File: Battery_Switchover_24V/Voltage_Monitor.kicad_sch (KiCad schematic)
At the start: 15 parts, among them Q2 NMOS, Q3 NMOS, Q4 NMOS, Q5 NMOS, Q6 NMOS, Q7 NMOS, U1 LM74610QDGKRQ1, U2 LM74610QDGKRQ1

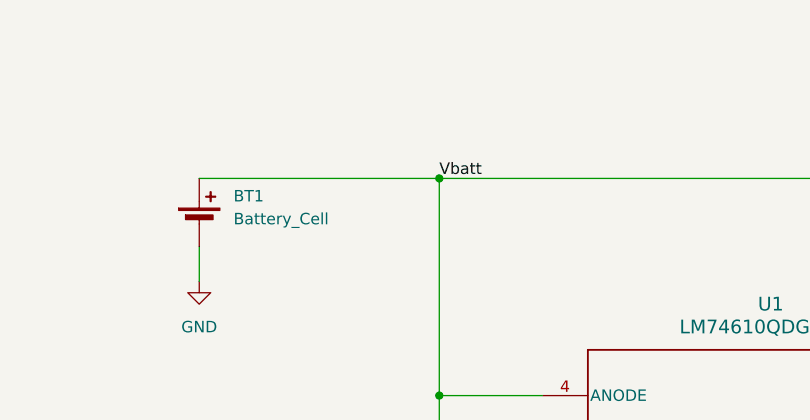
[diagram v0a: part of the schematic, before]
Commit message: Voltaj denetim çipi eklendi
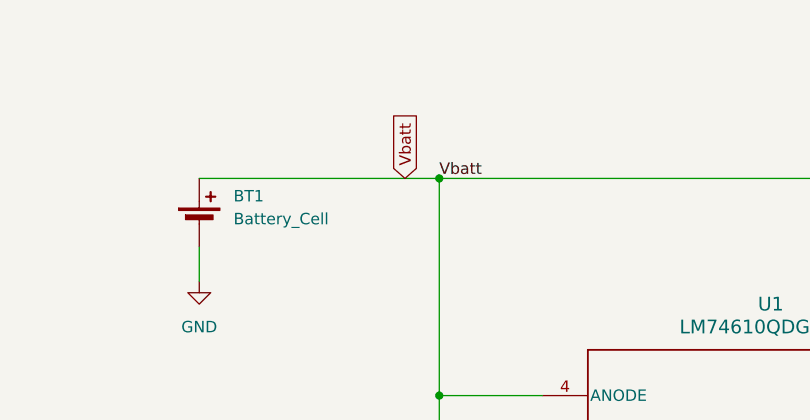
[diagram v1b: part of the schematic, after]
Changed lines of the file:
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@@
+		)
+	)
+	(global_label "Vbatt"
+		(shape input)
+		(at 147.32 33.02 90)
+		(fields_autoplaced yes)
+		(effects
+			(font
+				(size 1.27 1.27)
+			)
+			(justify left)
+		)
+		(property "Intersheetrefs" "${INTERSHEET_REFS}"
+			(at 147.32 25.1968 90)
+			(effects
+				(font
+					(size 1.27 1.27)
+				)
+				(justify left)
+				(hide yes)
+			)
 		)
 	)

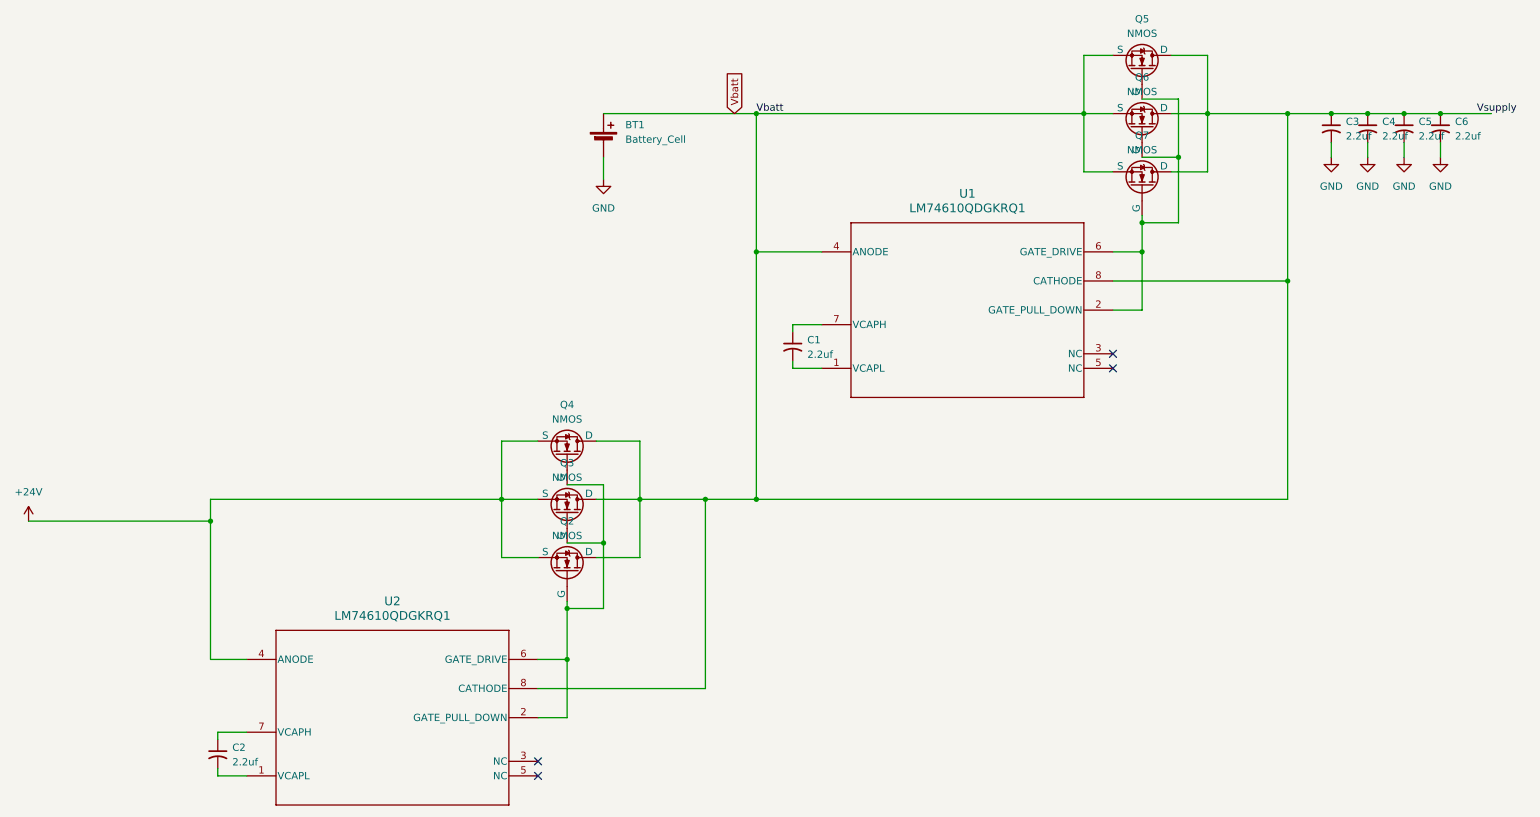
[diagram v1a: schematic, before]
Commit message: Changer Voltage Detection
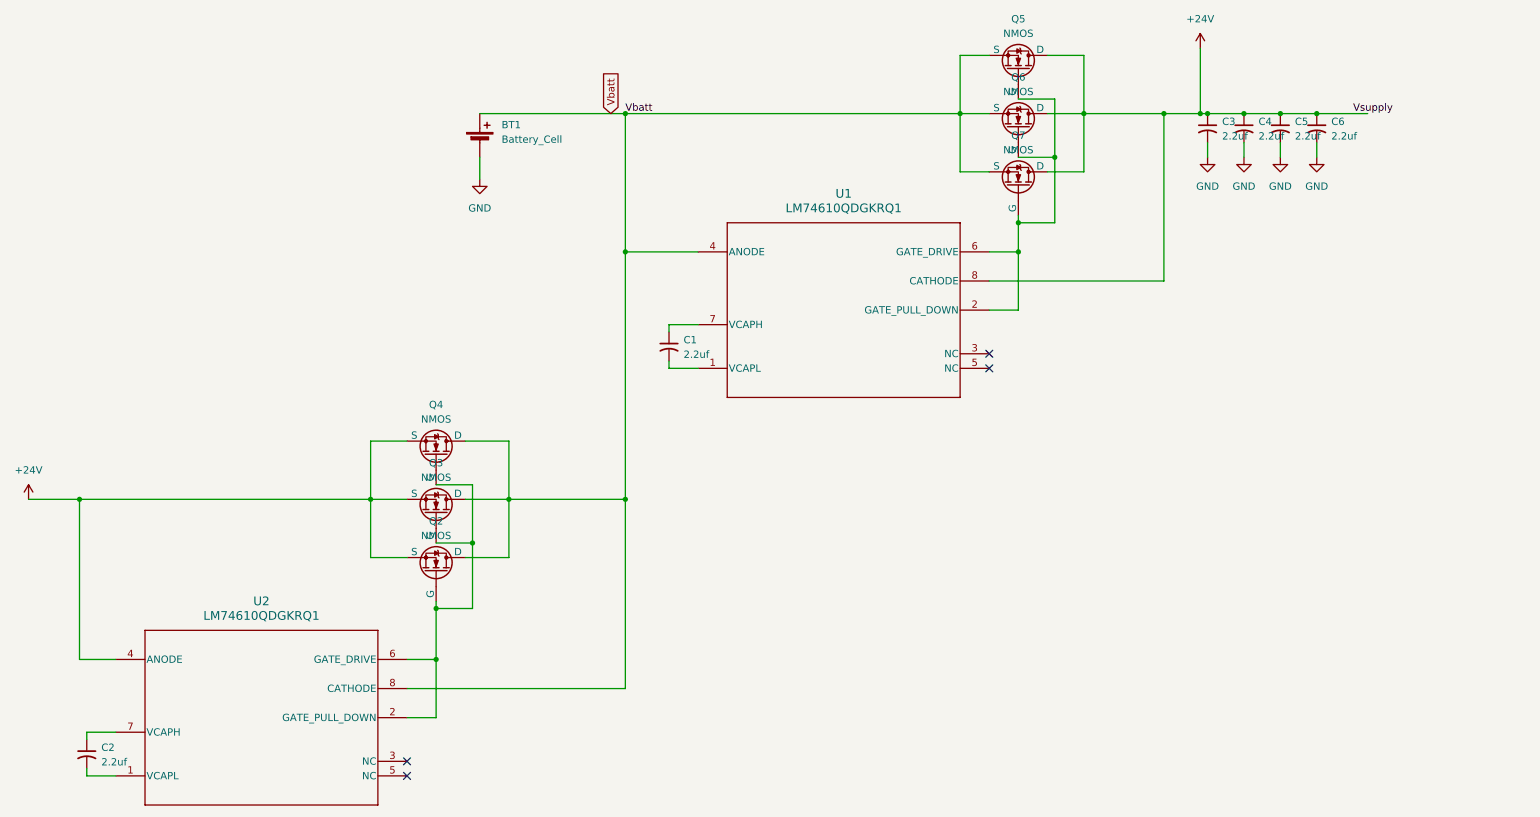
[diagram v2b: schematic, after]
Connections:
- net +24V: now also C3.1, C4.1, C5.1, C6.1, Q5.1 (D), Q6.1 (D), Q7.1 (D), U1.8 (CATHODE)
- net Vbatt: no longer C3.1, C4.1, C5.1, C6.1, Q5.1 (D), Q6.1 (D), Q7.1 (D), U1.8 (CATHODE)
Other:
- moved on the sheet: BT1, C1, C2, C3, C4, C5, C6, Q2, Q3, Q4, Q5, Q6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

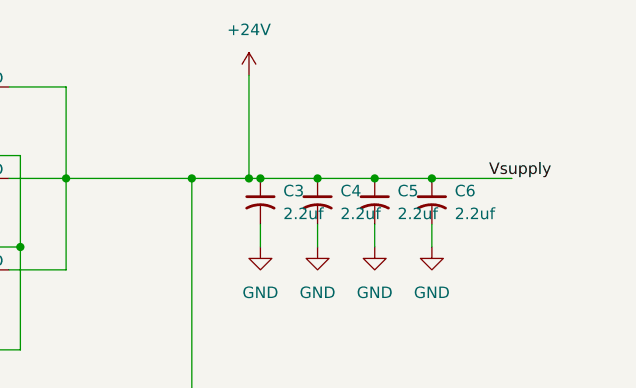
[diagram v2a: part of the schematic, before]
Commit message: Added USB connection
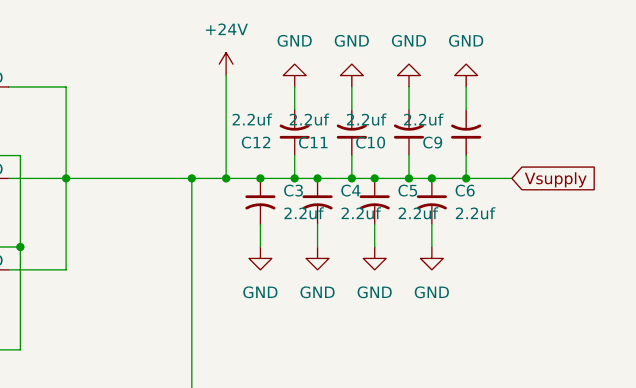
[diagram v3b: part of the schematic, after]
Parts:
- added C10, C11, C12, C9: 2.2uf, symbol Device:C_Small_US
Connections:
- net +24V: now also C10.1, C11.1, C12.1, C9.1
- net GND: now also C10.2, C11.2, C12.2, C9.2

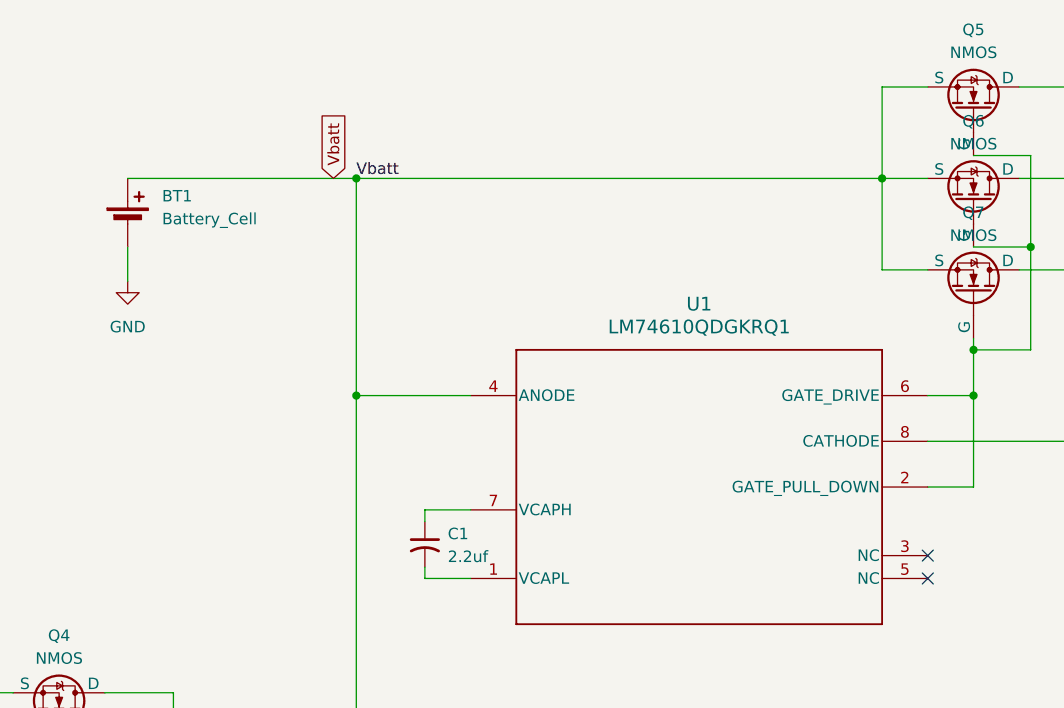
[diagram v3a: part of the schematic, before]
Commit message: Akım devresi eklendi Diğer devrelerde değişikler yapıldı
24 volttan tps54560 ile 5V oradan linear regulator ile 3.3V dönüştürüldü.

LPC11U14 e cristal eklendi
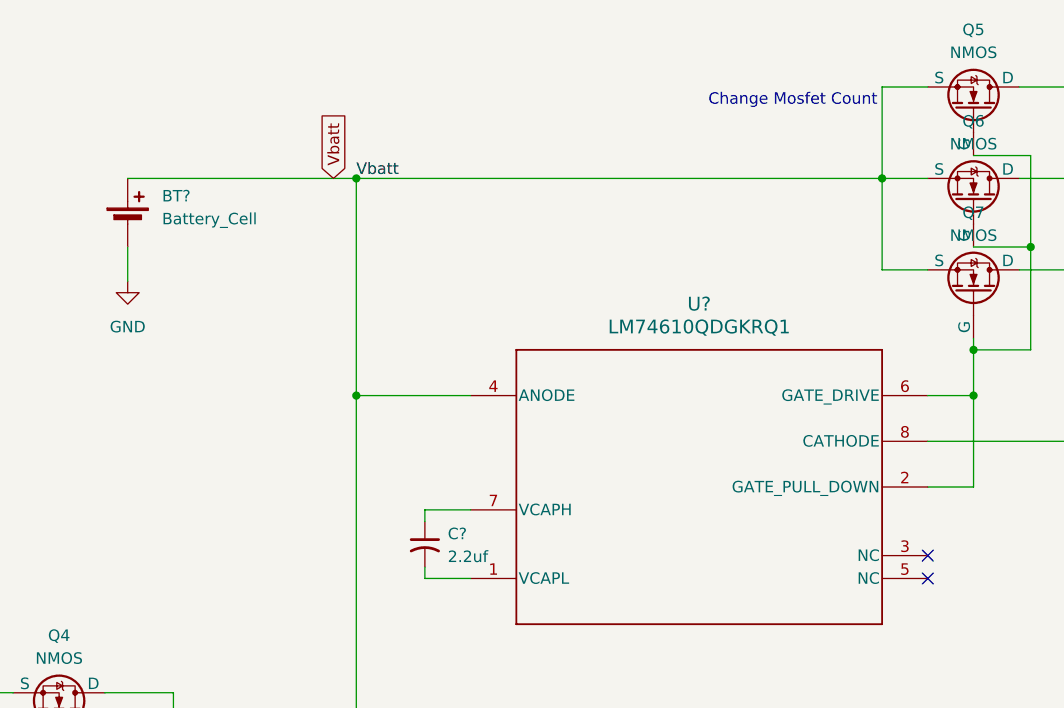
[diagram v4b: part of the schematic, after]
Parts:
- renumbered BT1 to BT?, C1 to C?, U1 to U?
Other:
- note added: "Change Mosfet Count"
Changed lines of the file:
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@@
 	(generator_version "9.0")
 	(paper "A4")
+	(text "Change Mosfet Count\n"
+		(exclude_from_sim no)
+		(at 176.784 24.384 0)
+		(effects
+			(font
+				(size 1.27 1.27)
+			)
+		)
+	)
 	(junction
 		(at 33.02 100.33)
@@
 		(dnp no)
 		(fields_autoplaced yes)
-		(property "Reference" "U1"
+		(property "Reference" "U?"
 			(at 166.37 46.99 0)
 			(effects
@@
 		)
 		(instances
-			(project ""
+			(project "Battery_Switchover_24V"
 				(path "/045845e0-5d00-4da8-961e-99bdf190f683/40a8593a-1917-4d96-a386-ebab07cd1c69"
-					(reference "U1")
+					(reference "U?")
 					(unit 1)
 				)
@@
 		(dnp no)
 		(fields_autoplaced yes)
-		(property "Reference" "#PWR01"
+		(property "Reference" "#PWR?"
 			(at 102.87 50.8 0)
 			(effects
@@
 		)
 		(instances
-			(project ""
+			(project "Battery_Switchover_24V"
 				(path "/045845e0-5d00-4da8-961e-99bdf190f683/40a8593a-1917-4d96-a386-ebab07cd1c69"
-					(reference "#PWR01")
+					(reference "#PWR?")
 					(unit 1)
 				)
@@
 		(dnp no)
 		(fields_autoplaced yes)
-		(property "Reference" "BT1"
+		(property "Reference" "BT?"
 			(at 106.68 34.9884 0)
 			(effects
@@
 		)
 		(instances
-			(project ""
+			(project "Battery_Switchover_24V"
 				(path "/045845e0-5d00-4da8-961e-99bdf190f683/40a8593a-1917-4d96-a386-ebab07cd1c69"
-					(reference "BT1")
+					(reference "BT?")
 					(unit 1)
 				)
@@
 		(dnp no)
 		(fields_autoplaced yes)
-		(property "Reference" "#PWR02"
+		(property "Reference" "#PWR?"
 			(at 24.13 104.14 0)
 			(effects
@@
 		)
 		(instances
-			(project ""
+			(project "Battery_Switchover_24V"
 				(path "/045845e0-5d00-4da8-961e-99bdf190f683/40a8593a-1917-4d96-a386-ebab07cd1c69"
-					(reference "#PWR02")
+					(reference "#PWR?")
 					(unit 1)
 				)
@@
 		(dnp no)
 		(fields_autoplaced yes)
-		(property "Reference" "C1"
+		(property "Reference" "C?"
 			(at 138.43 72.5169 0)
 			(effects
@@
 		)
 		(instances
-			(project ""
+			(project "Battery_Switchover_24V"
 				(path "/045845e0-5d00-4da8-961e-99bdf190f683/40a8593a-1917-4d96-a386-ebab07cd1c69"
-					(reference "C1")
+					(reference "C?")
 					(unit 1)
 				)
